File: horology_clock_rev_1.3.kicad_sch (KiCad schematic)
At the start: 40 parts, among them J1 Conn_01x36, J10 Conn_01x09, J11 Screw_Terminal_01x02, J12 Conn_01x02, J13 Conn_01x04, J2 Conn_01x36, J3 Screw_Terminal_01x02, J4 Screw_Terminal_01x02, J5 Screw_Terminal_01x02, J6 Conn_01x02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

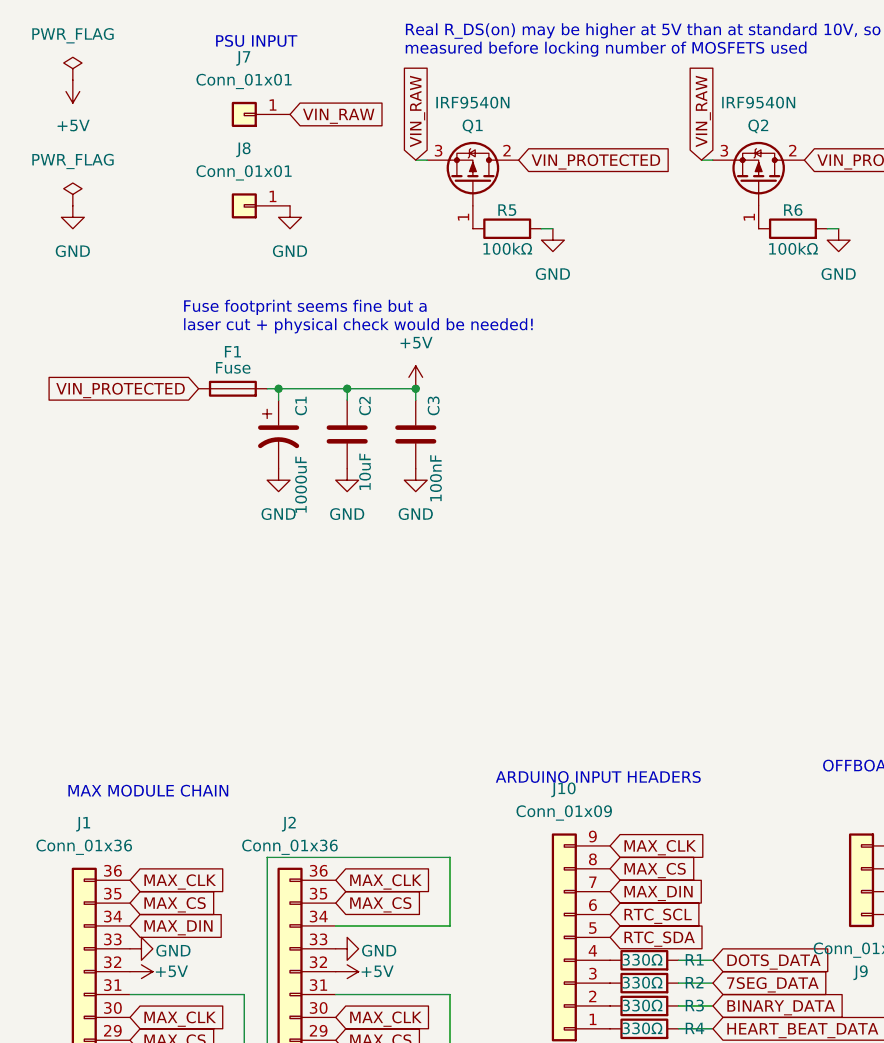
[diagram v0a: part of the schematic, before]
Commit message: completed main power distribution redesign - power connector on top right edge
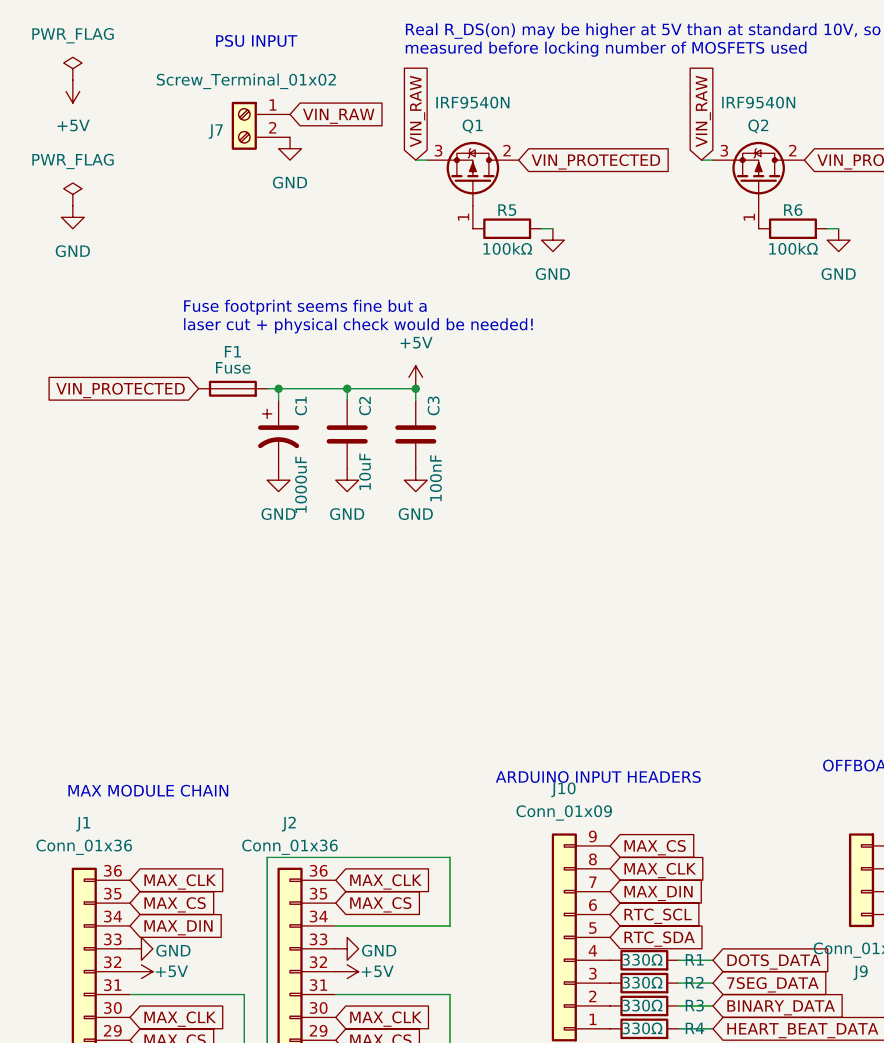
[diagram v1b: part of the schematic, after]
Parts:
- removed J7, J8: Conn_01x01, Connector_Wire:SolderWire-1sqmm_1x01_D1.4mm_OD3.9mm_Relief, symbol Connector_Generic:Conn_01x01
- added J7: Screw_Terminal_01x02, TerminalBlock:TerminalBlock_MaiXu_MX126-5.0-02P_1x02_P5.00mm, symbol Connector:Screw_Terminal_01x02
- R1, R2, R3, R4: footprint Resistor_THT:R_Axial_DIN0204_L3.6mm_D1.6mm_P5.08mm_Horizontal -> Resistor_THT:R_Axial_DIN0207_L6.3mm_D2.5mm_P10.16mm_Horizontal
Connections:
- net GND: now also J7.2 (Pin_2)
- net MAX_CLK: now also J10.8 (Pin_8); no longer J10.9 (Pin_9)
- net MAX_CS: now also J10.9 (Pin_9); no longer J10.8 (Pin_8)
- net VIN_RAW: now also J7.1 (Pin_1)

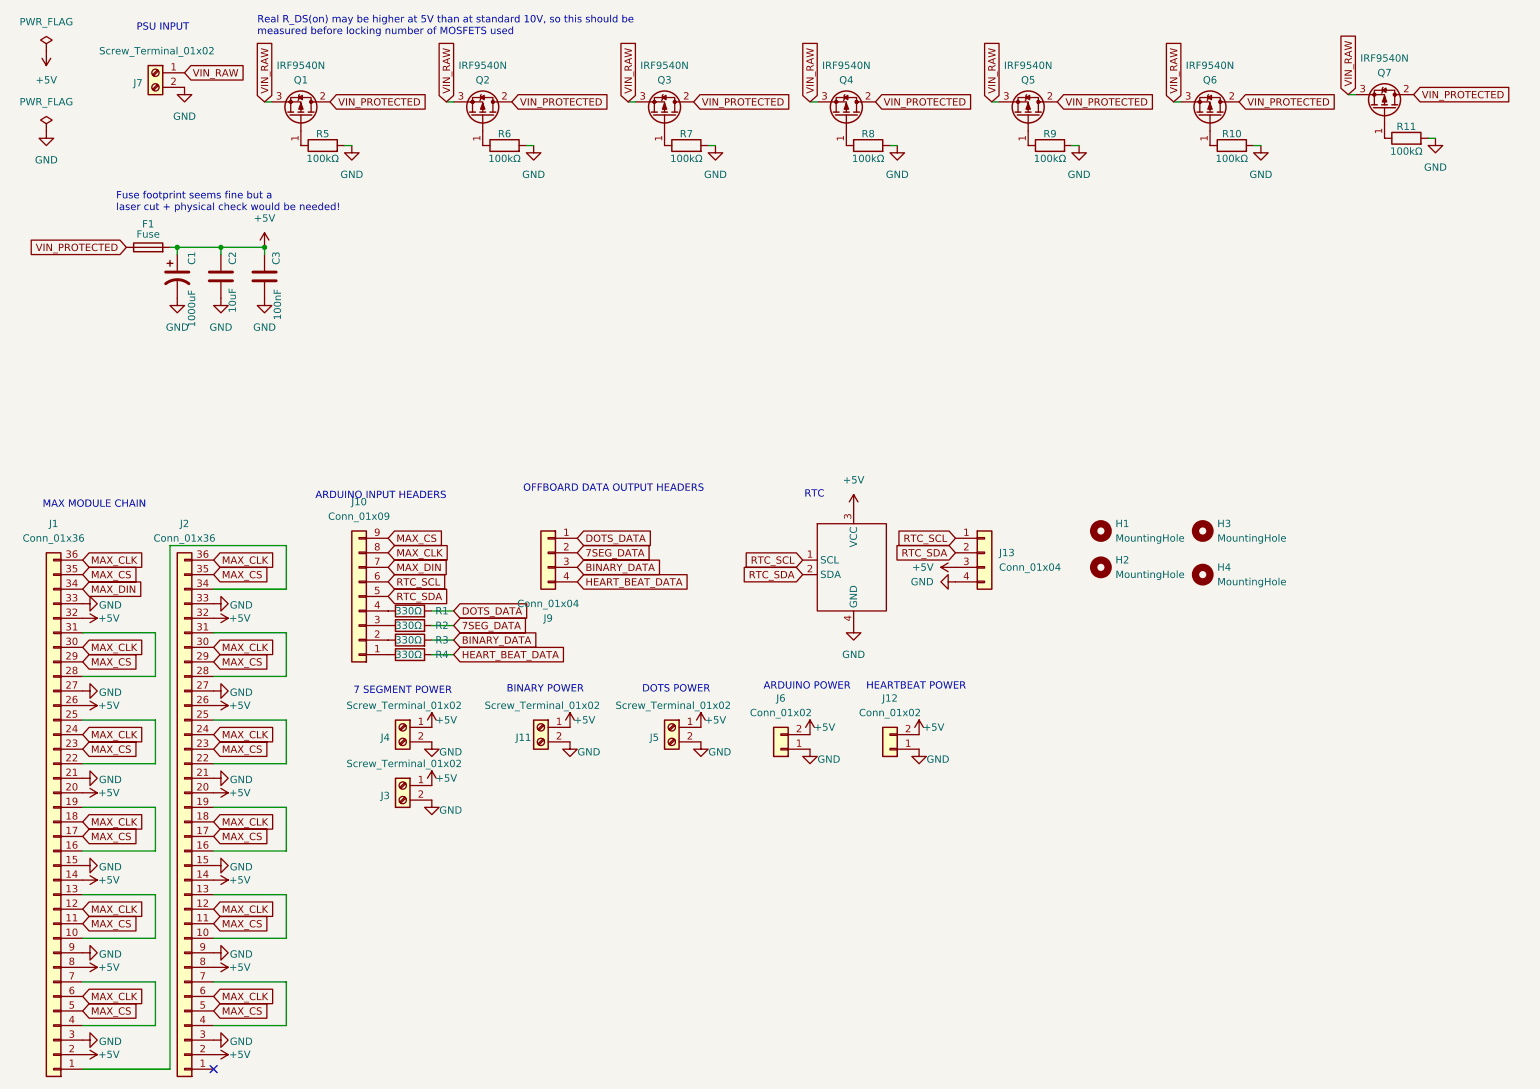
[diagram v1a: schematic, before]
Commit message: Added Arduino on underside. Arduino USB below main power plug.
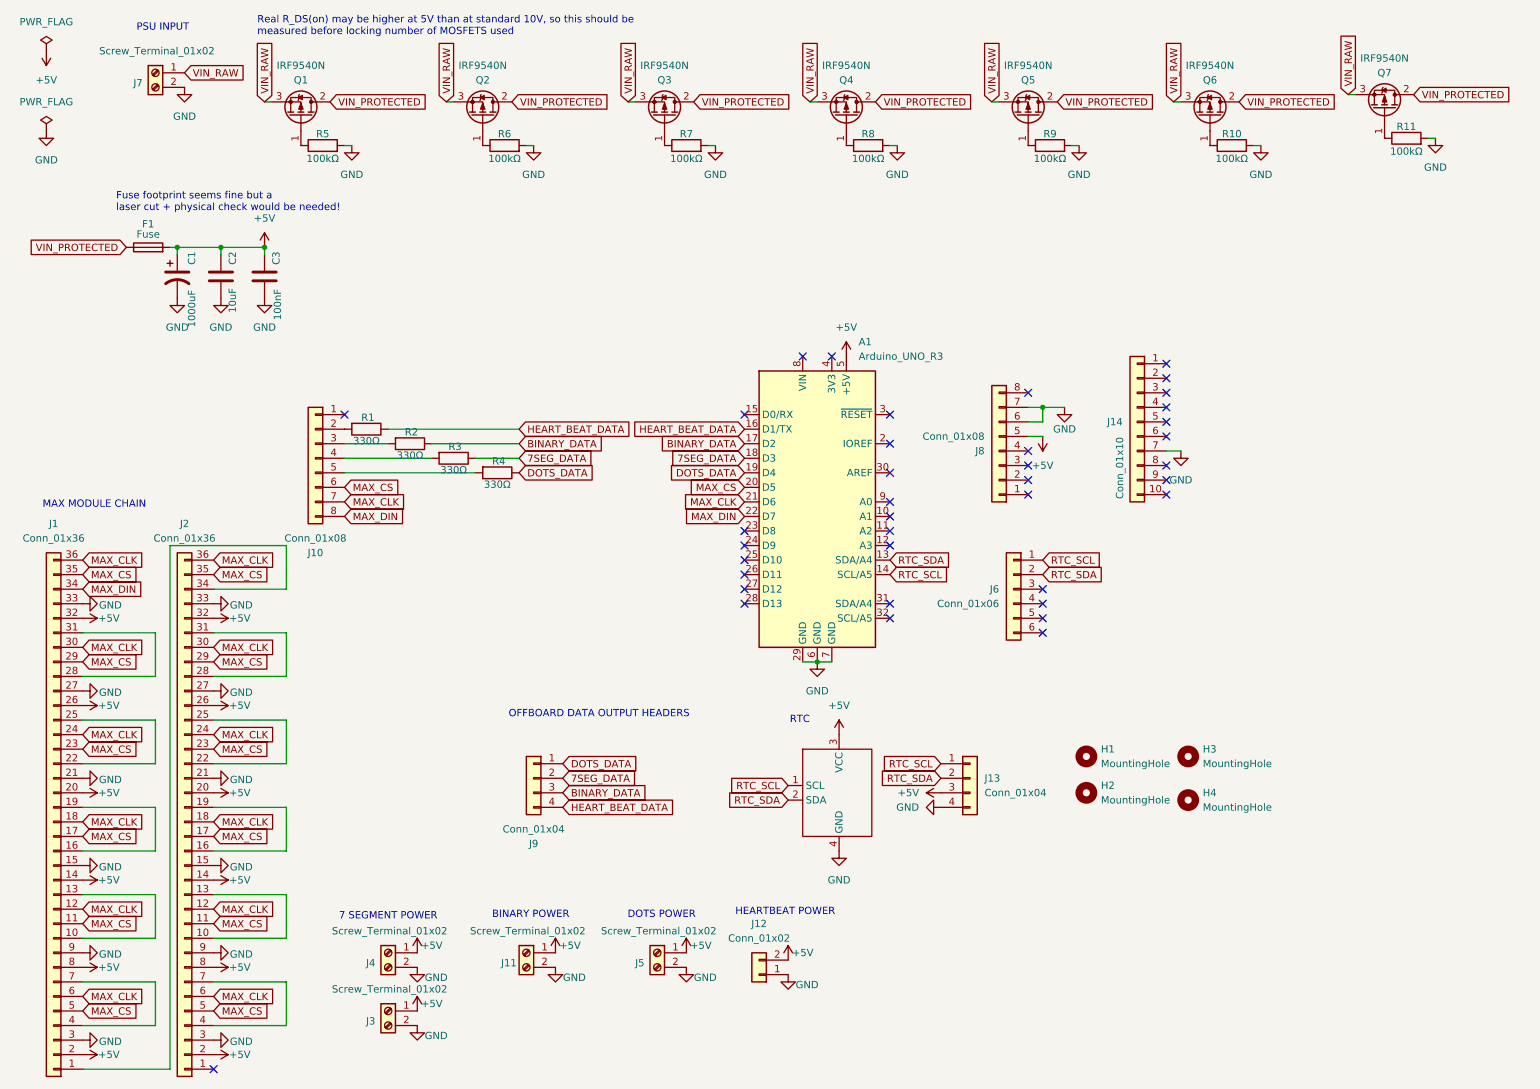
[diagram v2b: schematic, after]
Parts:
- removed J10: Conn_01x09, Connector_PinHeader_2.54mm:PinHeader_1x09_P2.54mm_Vertical, symbol Connector_Generic:Conn_01x09
- removed J6: Conn_01x02, Connector_PinHeader_2.54mm:PinHeader_1x02_P2.54mm_Vertical, symbol Connector_Generic:Conn_01x02
- added A1: Arduino_UNO_R3, Standoffed Arduino R3pretty:Arduino_UNO_R3_WithMountingHoles_Standoff_Mounted, symbol MCU_Module:Arduino_UNO_R3
- added J10, J8: Conn_01x08, Connector_PinHeader_2.54mm:PinHeader_1x08_P2.54mm_Vertical, symbol Connector_Generic:Conn_01x08
- added J14: Conn_01x10, Connector_PinHeader_2.54mm:PinHeader_1x10_P2.54mm_Vertical, symbol Connector_Generic:Conn_01x10
- added J6: Conn_01x06, Connector_PinHeader_2.54mm:PinHeader_1x06_P2.54mm_Vertical, symbol Connector_Generic:Conn_01x06
- F1: footprint Fuse:Fuseholder_Cylinder-5x20mm_Schurter_0031_8201_Horizontal_Open -> Custom Fuse:Fuseholder_Cylinder-5x20mm_Schurter_0031_8201_Horizontal_Open_No_Hole
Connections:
- net +5V: now also A1.5 (+5V), J8.5 (Pin_5)
- net 7SEG_DATA: now also R3.1, A1.18 (D3); no longer R2.2
- net BINARY_DATA: now also R2.1, A1.17 (D2); no longer R3.2
- net DOTS_DATA: now also R4.1, A1.19 (D4); no longer R1.2
- net GND: now also A1.29 (GND), A1.6 (GND), A1.7 (GND), J14.7 (RESET), J8.6 (Pin_6), J8.7 (Pin_7)
- net HEART_BEAT_DATA: now also R1.1, A1.16 (D1/TX); no longer R4.2
- net MAX_CLK: now also A1.21 (D6), J10.7 (Pin_7)
- net MAX_CS: now also A1.20 (D5), J10.6 (Pin_6)
- net MAX_DIN: now also A1.22 (D7), J10.8 (Pin_8)
- net RTC_SCL: now also A1.14 (SCL/A5), J6.1 (Pin_1)
- net RTC_SDA: now also A1.13 (SDA/A4), J6.2 (Pin_2)
- new net: J10.2 (Pin_2), R1.2
- new net: J10.3 (Pin_3), R2.2
- new net: J10.4 (Pin_4), R3.2
- new net: J10.5 (Pin_5), R4.2
- no-connect marks 1 -> 38
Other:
- note removed: "ARDUINO INPUT HEADERS"
- note removed: "ARDUINO POWER"
- moved on the sheet: H1, H2, H3, H4, J11, J12, J13, J3, J4, J5, J9, R4

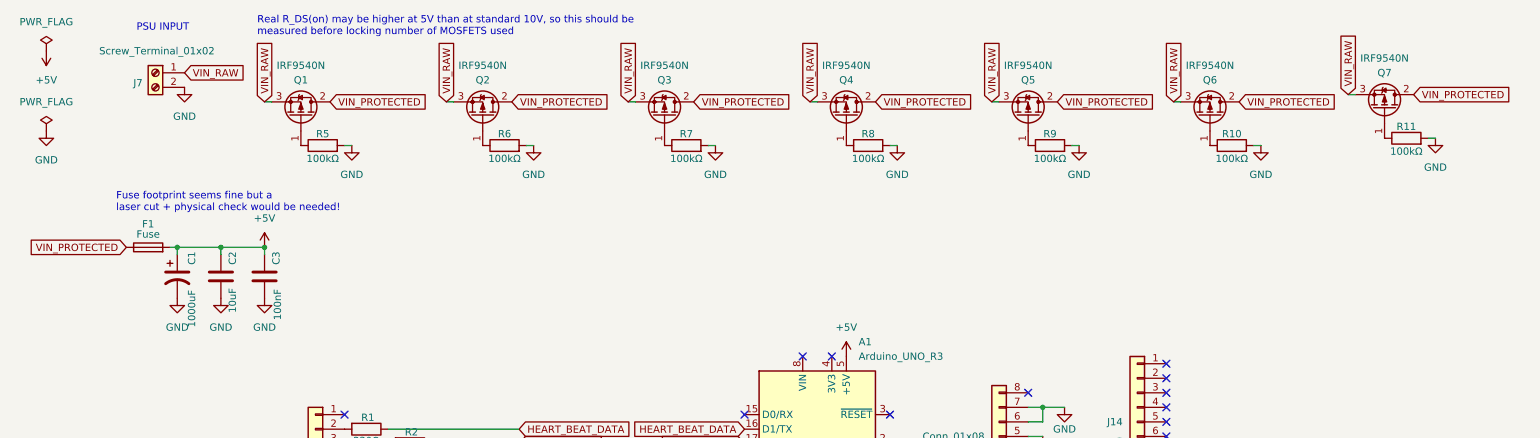
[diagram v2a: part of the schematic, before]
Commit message: Corrected Power Order: Now POWER -> FUSE -> MOSFETS
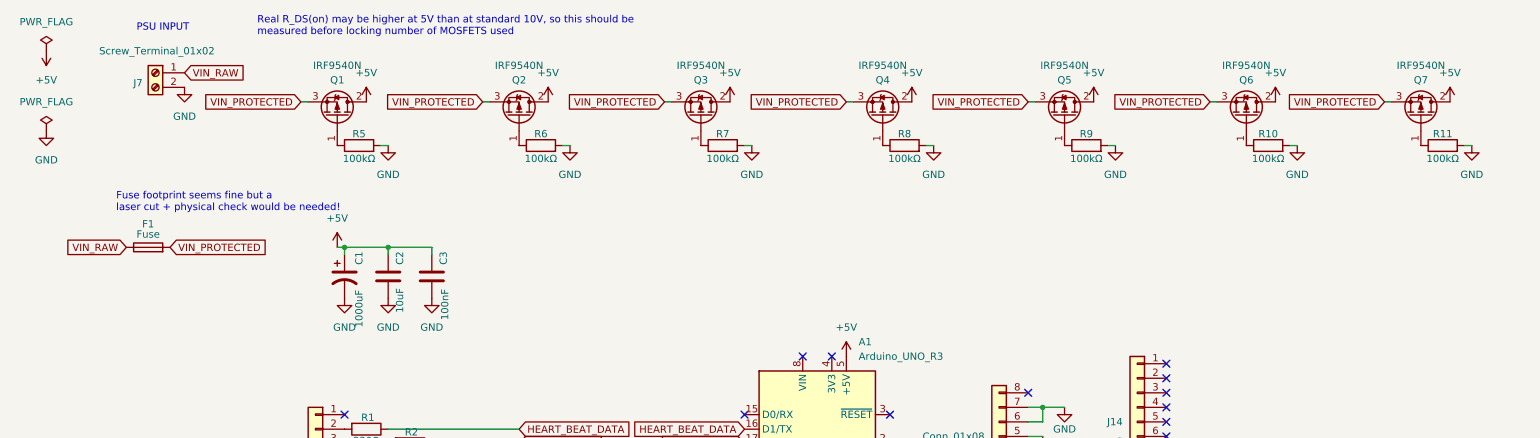
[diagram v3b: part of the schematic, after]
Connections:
- net +5V: now also Q1.2 (D), Q2.2 (D), Q3.2 (D), Q4.2 (D), Q5.2 (D), Q6.2 (D), Q7.2 (D); no longer F1.2
- net VIN_PROTECTED: now also F1.2, Q1.3 (S), Q2.3 (S), Q3.3 (S), Q4.3 (S), Q5.3 (S), Q6.3 (S), Q7.3 (S); no longer F1.1, Q1.2 (D), Q2.2 (D), Q3.2 (D), Q4.2 (D), Q5.2 (D), Q6.2 (D), Q7.2 (D)
- net VIN_RAW: now also F1.1; no longer Q1.3 (S), Q2.3 (S), Q3.3 (S), Q4.3 (S), Q5.3 (S), Q6.3 (S), Q7.3 (S)
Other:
- moved on the sheet: C1, C2, C3, Q1, Q2, Q3, Q4, Q5, Q6, Q7, R10, R11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

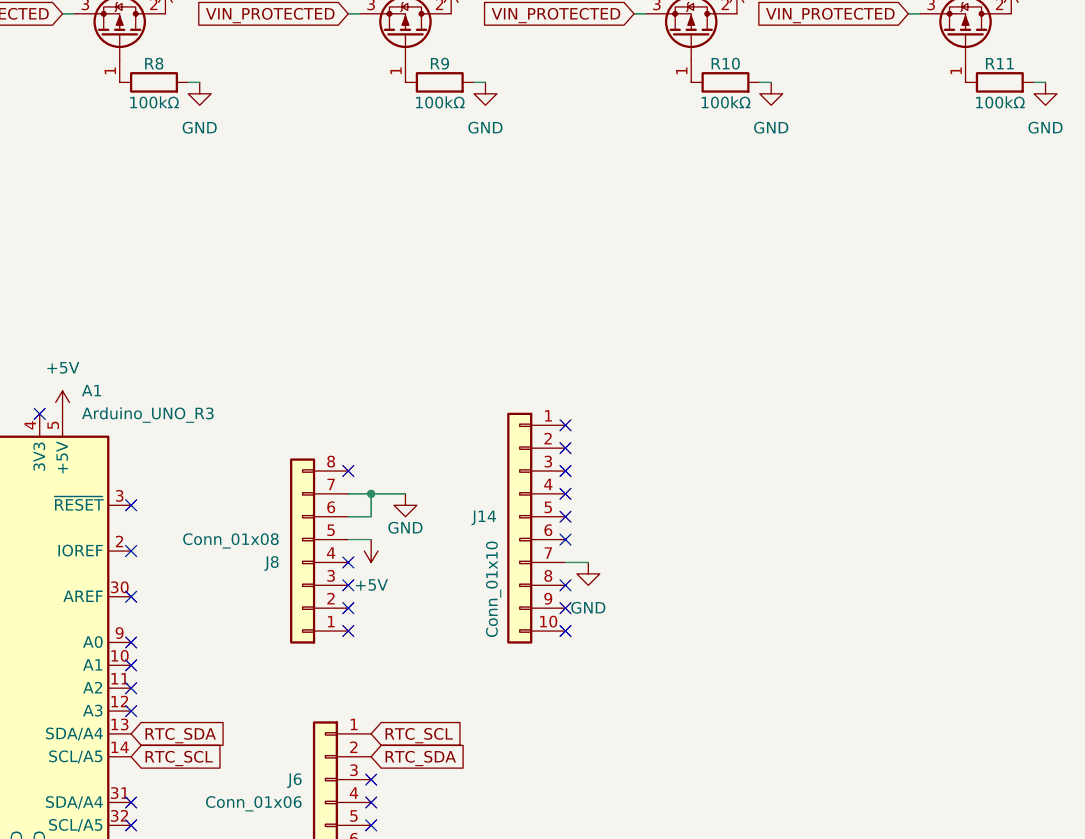
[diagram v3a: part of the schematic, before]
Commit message: Moved Arduino such that mounting holes for all components dont intersect other each others footprints.
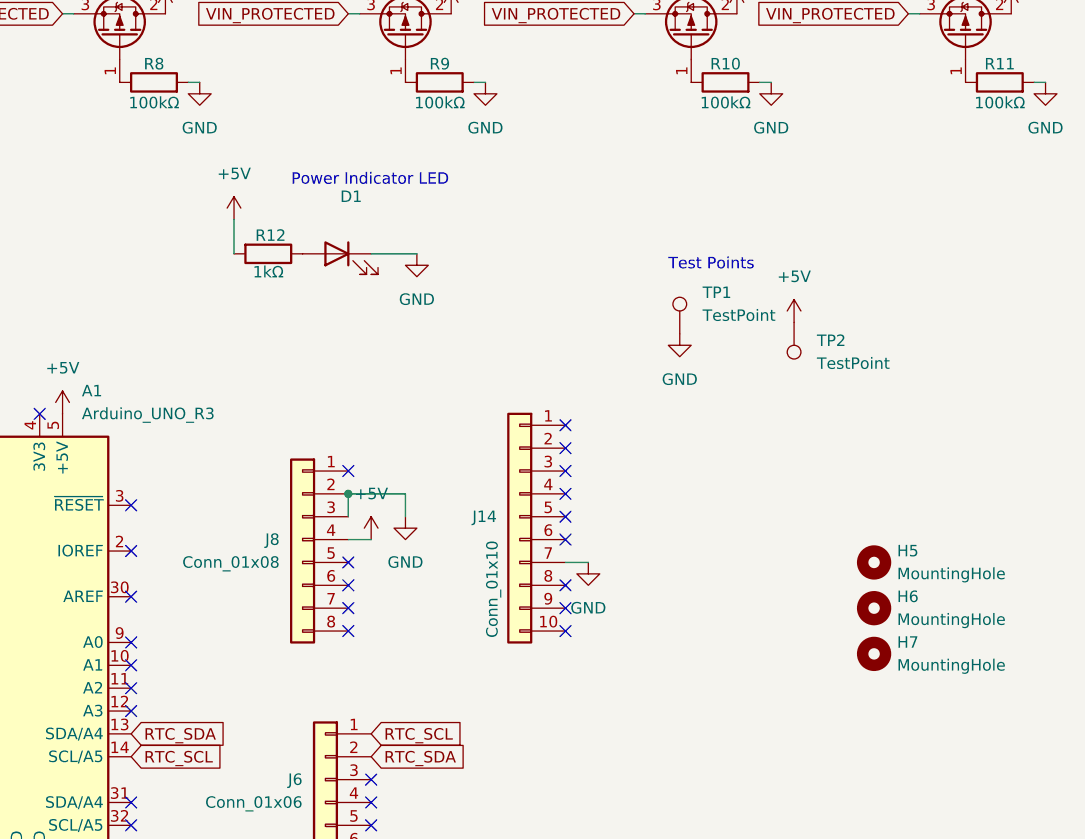
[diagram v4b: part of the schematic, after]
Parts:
- added D1: LED, LED_THT:LED_D5.0mm, symbol Device:LED
- added H5, H6, H7: MountingHole, symbol Mechanical:MountingHole
- added R12: 1kΩ, Resistor_THT:R_Axial_DIN0207_L6.3mm_D2.5mm_P10.16mm_Horizontal, symbol Device:R
- added TP1: TestPoint, TestPoint:TestPoint_Pad_2.5x2.5mm, symbol Connector:TestPoint
- added TP2: TestPoint, TestPoint:TestPoint_Pad_2.0x2.0mm, symbol Connector:TestPoint
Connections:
- net +5V: now also J8.4 (Pin_4), R12.2, TP2.1; no longer J8.5 (Pin_5)
- net GND: now also J8.2 (Pin_2), J8.3 (Pin_3), D1.1 (K), TP1.1; no longer J8.6 (Pin_6), J8.7 (Pin_7)
- new net: D1.2 (A), R12.1
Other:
- note added: "Power Indicator LED"
- note added: "Test Points"
- moved on the sheet: J8
